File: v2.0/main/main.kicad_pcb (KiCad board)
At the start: 2 copper layers, 61 x 38 mm, 107 parts, among them J1 enc_host, J2 enc_slave, J3 motor_L, J4 motor_R, J5 Battery, J6 enc_host, J7 enc_slave, J8 Conn_ARM_JTAG_SWD_10, J9 Conn_01x02, Q1 LTR-209, Q2 IRLML6402, Q3 BSS138, Q4 LTR-209, Q5 LTR-209, Q6 LTR-209, Q7 PMF250XNEX, Q8 PMF250XNEX, Q9 IRFML8244, SW1 TVAF06-A020B-R, SW2 EG1215AA, SW3 TVAF06-A020B-R, U1 STM32F411CEUx, U2 MA730, U3 ICM-20600, U4 DRV8835, U5 TLV75733PDBV, U6 MA730

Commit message: feat: update pcb routing
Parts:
- removed the C1 at (164.3, 69.3)
- removed the C19 at (163.5, 134.8)
- removed the C2 at (164.3, 71.3)
- removed the D10 at (192.8, 103.8)
- removed the D11 at (193.0, 88.9)
- removed the J1 at (166.8, 103.1)
- removed the J6 at (162.8, 91.2)
- removed L3: 10u, Inductor_SMD:L_0805_2012Metric
- removed the Q7 at (188.0, 88.7)
- removed Q8: PMF250XNEX, Package_TO_SOT_SMD:SOT-323_SC-70_Handsoldering
- removed the R1 at (164.3, 67.3)
- removed the R10 at (159.8, 135.0)
- removed the R23 at (194.4, 100.3)
- removed the R30 at (185.2, 102.6)
- removed the R31 at (186.5, 105.5)
- added C16: 0.1u, Capacitor_SMD:C_0402_1005Metric, F.Cu at (191.1, 94.3)
- added C21: 0.1u, Capacitor_SMD:C_0402_1005Metric, F.Cu at (191.1, 100.5)
- added C22: 0.1u, Capacitor_SMD:C_0402_1005Metric, F.Cu at (177.2, 86.1)
- added C23: 0.1u, Capacitor_SMD:C_0402_1005Metric, F.Cu at (177.1, 110.3)
- added C24: 1u, Capacitor_SMD:C_0402_1005Metric, F.Cu at (177.7, 82.8)
- added C25: 1u, Capacitor_SMD:C_0402_1005Metric, F.Cu at (190.1, 91.3)
- added C8: 0.1u, Capacitor_SMD:C_0201_0603Metric, F.Cu at (152.6, 99.2)
- added D14: OSI5FU3A11C, half_mouse_lib:OSI5FU3A11C, F.Cu at (191.3, 90.5)
- added D15: OSI5FU3A11C, half_mouse_lib:OSI5FU3A11C, F.Cu at (191.4, 103.2)
- added R35: 8.2, Resistor_SMD:R_0402_1005Metric, F.Cu at (189.1, 105.4)
- added R36: 8.2, Resistor_SMD:R_0402_1005Metric, F.Cu at (189.0, 88.0)
- added R4: 1.5k, Resistor_SMD:R_0402_1005Metric, F.Cu at (192.1, 94.3)
- added U7: BCR421UW6-7, Package_TO_SOT_SMD:SOT-23-6, F.Cu at (186.4, 105.8)
- added U8: BCR421UW6-7, Package_TO_SOT_SMD:SOT-23-6, F.Cu at (186.3, 88.4)
- C15: renamed from C16; footprint Capacitor_SMD:C_0603_1608Metric -> Capacitor_SMD:C_0402_1005Metric
- J1, J6: footprint Connector_PinHeader_1.27mm:PinHeader_1x04_P1.27mm_Vertical -> half_mouse_lib:enc_fp
- J2, J7: footprint half_mouse_lib:encoder_board -> half_mouse_lib:enc_board
- J3, J4: footprint half_mouse_lib:motor_SMD -> Connector_PinHeader_1.00mm:PinHeader_1x02_P1.00mm_Vertical
- J9: footprint Connector_PinSocket_1.27mm:PinSocket_1x02_P1.27mm_Vertical -> Connector_PinHeader_1.00mm:PinHeader_1x02_P1.00mm_Vertical
- Q1, Q4, Q5, Q6: value LTR-209 -> OP505A
- R24, R26: value 1k -> 1.5k; footprint Resistor_SMD:R_0201_0603Metric -> Resistor_SMD:R_0402_1005Metric
- R25, R27, R29, R5: value 1k -> 10k; footprint Resistor_SMD:R_0201_0603Metric -> Resistor_SMD:R_0402_1005Metric
- R28: value 10 -> 1.5k; footprint Resistor_SMD:R_0201_0603Metric -> Resistor_SMD:R_0402_1005Metric
- R7: value 10k -> 6.8k
- R8: value 10k -> 15k
- SP1: footprint omni:STM0440-T-R -> half_mouse_lib:SMT-0440-T-HT-R
- moved D8 56.8 mm to (134.6, 100.8)
- moved D7 55.3 mm to (134.6, 99.3)
- moved R18 54.6 mm to (136.5, 100.8), turned to 180 degrees
- moved R17 53.3 mm to (136.5, 99.3), turned to 180 degrees
- moved R20 52.3 mm to (136.5, 103.7), turned to 180 degrees
- moved R21 52.1 mm to (136.5, 105.2), turned to 180 degrees
- moved D10 51.8 mm to (134.6, 103.7)
- moved D11 51.3 mm to (134.6, 105.2)
- moved D9 43.9 mm to (134.6, 102.2)
- moved D6 43.2 mm to (134.6, 95.5), turned to 0 degrees
- moved R19 41.8 mm to (136.5, 102.2), turned to 180 degrees
- moved R11 41.2 mm to (167.1, 79.5), turned to -90 degrees
- moved R16 41.1 mm to (136.5, 95.5)
- moved J1 37.0 mm to (164.7, 105.4), turned to 180 degrees
- moved R10 36.9 mm to (164.5, 83.2)
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- renumbered C3 to C1, C11 to C10, C12 to C11, C13 to C12, C14 to C13, C15 to C14, C20 to C19, C4 to C2, C21 to C20, C5 to C3, C6 to C4, C7 to C5, C8 to C6, C9 to C7, C10 to C9, D14 to D10, D15 to D11, Q9 to Q7, R2 to R1, R11 to R10, R12 to R11, R13 to R12, R14 to R13, R15 to R14, R16 to R15, R17 to R16, R18 to R17, R19 to R18, R20 to R19, R3 to R2, R37 to R20, R38 to R21, R21 to R22, R22 to R23, R4 to R3, R32 to R30, R33 to R31, R34 to R32, R35 to R33, R36 to R34
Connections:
- J2 pad 2: /encoder_R/s_MISO -> ENC_R_B
- J2 pad 3: /encoder_R/s_MOSI -> ENC_R_A
- J2 pad 4: /encoder_R/s_CS -> /encoder_R/s_GND
- J7 pad 2: /encoder_L/s_MISO -> ENC_L_B
- J7 pad 3: /encoder_L/s_MOSI -> ENC_L_A
- J7 pad 4: /encoder_L/s_CS -> /encoder_L/s_GND
- L2 pad 1: Net-(U4-BOUT2) -> Net-(U4-BOUT1)
- L2 pad 2: Net-(J4-Pin_2) -> Net-(J4-Pin_1)
- Q1 pad 1: +3.3VADC -> +3.3V
- Q1 pad 2: IR_RCV_FL -> Net-(Q1-E)
- Q4 pad 1: +3.3VADC -> +3.3V
- Q4 pad 2: IR_RCV_FR -> Net-(Q4-E)
- Q5 pad 1: +3.3VADC -> +3.3V
- Q5 pad 2: IR_RCV_SL -> Net-(Q5-E)
- Q6 pad 1: +3.3VADC -> +3.3V
- Q6 pad 2: IR_RCV_SR -> Net-(Q6-E)
- R24 pad 1: IR_RCV_SL -> Net-(Q4-E)
- R25 pad 1: IR_RCV_SR -> IR_RCV_FR
- R26 pad 1: IR_LED_F -> Net-(Q5-E)
- R26 pad 2: Net-(Q7-G) -> GND
- R27 pad 1: Net-(Q7-G) -> IR_RCV_SL
- R28 pad 1: Net-(D11-K) -> Net-(Q6-E)
- R28 pad 2: Net-(Q7-D) -> GND
- R29 pad 1: IR_LED_S -> IR_RCV_SR
- R29 pad 2: Net-(Q8-G) -> GND
- U1 pad 16: IR_LED_F -> IR_LED_S
- U1 pad 19: IR_LED_S -> IR_LED_F
- U1 pad 2: USER_LED8 -> USER_LED7
- U1 pad 20: USER_LED1 -> unconnected-(U1-PB2-Pad20)
- U1 pad 21: USER_LED2 -> unconnected-(U1-PB10-Pad21)
- U1 pad 3: USER_LED9 -> USER_LED8
- U1 pad 31: USER_LED3 -> USER_LED1
- U1 pad 32: USER_LED4 -> USER_LED2
- U1 pad 33: USER_SW -> USER_LED3
- U1 pad 38: USER_LED5 -> USER_LED4
- U1 pad 39: USER_LED6 -> USER_LED5
- U1 pad 4: USER_LED10 -> USER_LED9
- U1 pad 40: USER_LED7 -> USER_LED6
- U1 pad 5: /OSC_IN -> USER_LED10
- U1 pad 6: /OSC_OUT -> USER_SW
- U1 pad 9: +3.3VADC -> +3.3V
- U4 pad 4: Net-(J4-Pin_1) -> Net-(U4-BOUT1)
- U4 pad 5: Net-(U4-BOUT2) -> Net-(J4-Pin_2)
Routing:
- net +3.3V: track 0.00 -> 217.4 mm, vias 0 -> 5
- net GND: track 0.00 -> 87.5 mm, vias 0 -> 33
- net Net-(D12-K): track 0.00 -> 57.0 mm
- net NRST: track 0.00 -> 52.0 mm, vias 0 -> 2
- net IR_LED_F: track 0.00 -> 42.5 mm
- net +BATT: track 0.00 -> 41.8 mm
- net IR_RCV_FL: track 0.00 -> 40.8 mm, vias 0 -> 2
- net IR_RCV_FR: track 0.00 -> 38.5 mm, vias 0 -> 2
- net IR_RCV_SL: track 0.00 -> 30.9 mm, vias 0 -> 2
- net IR_LED_S: track 0.00 -> 30.9 mm
- net FAN_MOTOR: track 0.00 -> 29.9 mm
- net USER_LED1: track 0.00 -> 29.9 mm, vias 0 -> 2
- net USER_LED2: track 0.00 -> 28.8 mm, vias 0 -> 2
- net USER_LED3: track 0.00 -> 28.4 mm, vias 0 -> 2
- net USER_SPEAKER: track 0.00 -> 27.2 mm, vias 0 -> 2
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- added copper zone on F.Cu, net +3.3V
- added copper zone on F.Cu, net +BATT
- added copper zone on B.Cu, net GND
- added copper zone on F.Cu, net GND
- removed copper zone on B.Cu, net /encoder_L/s_GND
- removed copper zone on F.Cu, net /encoder_L/s_GND
- removed copper zone on B.Cu, net /encoder_R/s_GND
- removed copper zone on F.Cu, net /encoder_R/s_GND
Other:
- board size 61 x 38 mm -> 68 x 38 mm

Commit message: feat: add vias
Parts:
- moved D15 0.71 mm to (191.4, 102.5)
- moved Q4 0.71 mm to (194.1, 100.2)
- moved R24 0.71 mm to (192.1, 99.8)
- moved R25 0.71 mm to (191.6, 98.3)
- moved C21 0.71 mm to (191.0, 99.8)
- moved C16 0.60 mm to (191.1, 94.9)
- moved C25 0.60 mm to (190.1, 92.0)
- moved D14 0.60 mm to (191.3, 91.1)
- moved Q1 0.60 mm to (194.1, 93.5)
- moved R4 0.60 mm to (192.1, 94.9)
- moved R5 0.60 mm to (191.6, 96.4)
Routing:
- net +3.3V: track 217.4 -> 229.0 mm, vias 5 -> 6
- net GND: track 87.5 -> 95.1 mm, vias 33 -> 218
- net Net-(D14-K): track 14.9 -> 13.5 mm
- net Net-(D12-K): track 57.0 -> 58.0 mm
- net SYS_JTMS_SWDIO: track 13.2 -> 13.9 mm
- net +BATT: track 41.8 -> 42.5 mm
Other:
- outline, holes or cut-outs redrawn

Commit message: fix: parts position
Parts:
- moved R11 4.49 mm to (163.6, 76.8), turned to 180 degrees
- moved R29 4.34 mm to (178.2, 107.5), turned to -90 degrees
- moved C23 4.23 mm to (179.7, 107.0), turned to 0 degrees
- moved J2 3.95 mm to (162.0, 120.4), turned to 180 degrees
- moved J7 3.54 mm to (162.0, 74.4), turned to 0 degrees
- moved C9 3.26 mm to (159.4, 114.4)
- moved R3 3.26 mm to (159.4, 116.5)
- moved U2 3.26 mm to (162.1, 115.5)
- moved C22 2.98 mm to (179.7, 87.8), turned to 0 degrees
- moved C19 2.78 mm to (164.6, 80.4)
- moved R10 2.78 mm to (162.0, 81.9)
- moved U6 2.78 mm to (162.1, 79.3)
- moved R28 2.74 mm to (179.7, 108.0), turned to 180 degrees
- moved R27 2.70 mm to (178.1, 87.3), turned to 90 degrees
- moved R2 2.67 mm to (162.1, 112.9), turned to 180 degrees
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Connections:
- J1 pad 2: ENC_R_A -> ENC_R_B
- J1 pad 3: ENC_R_B -> ENC_R_A
- J2 pad 1: /encoder_R/s_VDD -> /encoder_R/s_GND
- J2 pad 2: ENC_R_B -> /encoder_R/ENC_A_
- J2 pad 3: ENC_R_A -> /encoder_R/ENC_B_
- J2 pad 4: /encoder_R/s_GND -> /encoder_R/s_VDD
- J6 pad 2: ENC_L_A -> ENC_L_B
- J6 pad 3: ENC_L_B -> ENC_L_A
- J7 pad 1: /encoder_L/s_VDD -> /encoder_L/s_GND
- J7 pad 2: ENC_L_B -> /encoder_L/ENC_A_
- J7 pad 3: ENC_L_A -> /encoder_L/ENC_B_
- J7 pad 4: /encoder_L/s_GND -> /encoder_L/s_VDD
- U2 pad 2: ENC_R_A -> /encoder_R/ENC_A_
- U2 pad 6: ENC_R_B -> /encoder_R/ENC_B_
- U6 pad 2: ENC_L_A -> /encoder_L/ENC_A_
- U6 pad 6: ENC_L_B -> /encoder_L/ENC_B_
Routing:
- net /encoder_R/s_GND: track 0.00 -> 15.0 mm, vias 0 -> 18
- net /encoder_R/s_VDD: track 0.00 -> 7.25 mm
- net /encoder_L/s_GND: track 3.84 -> 9.15 mm, vias 4 -> 16
- net /encoder_L/s_VDD: track 1.81 -> 7.02 mm
- net /encoder_R/ENC_B_: track 0.00 -> 5.19 mm
- net /encoder_L/ENC_B_: track 0.00 -> 5.17 mm
- net ENC_L_B: track 10.3 -> 6.73 mm
- net +3.3V: track 229.0 -> 225.5 mm, vias 6 -> 7
- net /encoder_R/ENC_A_: track 0.00 -> 3.34 mm
- net ENC_R_A: track 19.7 -> 16.4 mm
- net /encoder_L/ENC_A_: track 0.00 -> 3.25 mm
- net FAN_MOTOR: track 29.9 -> 32.9 mm
- net Net-(Q2-G): track 6.86 -> 4.16 mm
- net Net-(Q3-D): track 3.54 -> 5.98 mm
- net USER_SPEAKER: track 27.2 -> 29.5 mm
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- added copper zone on B.Cu, net /encoder_L/s_GND
- added copper zone on F.Cu, net /encoder_L/s_GND
- added copper zone on B.Cu, net /encoder_R/s_GND
- added copper zone on F.Cu, net /encoder_R/s_GND
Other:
- board size 68 x 38 mm -> 68 x 48 mm

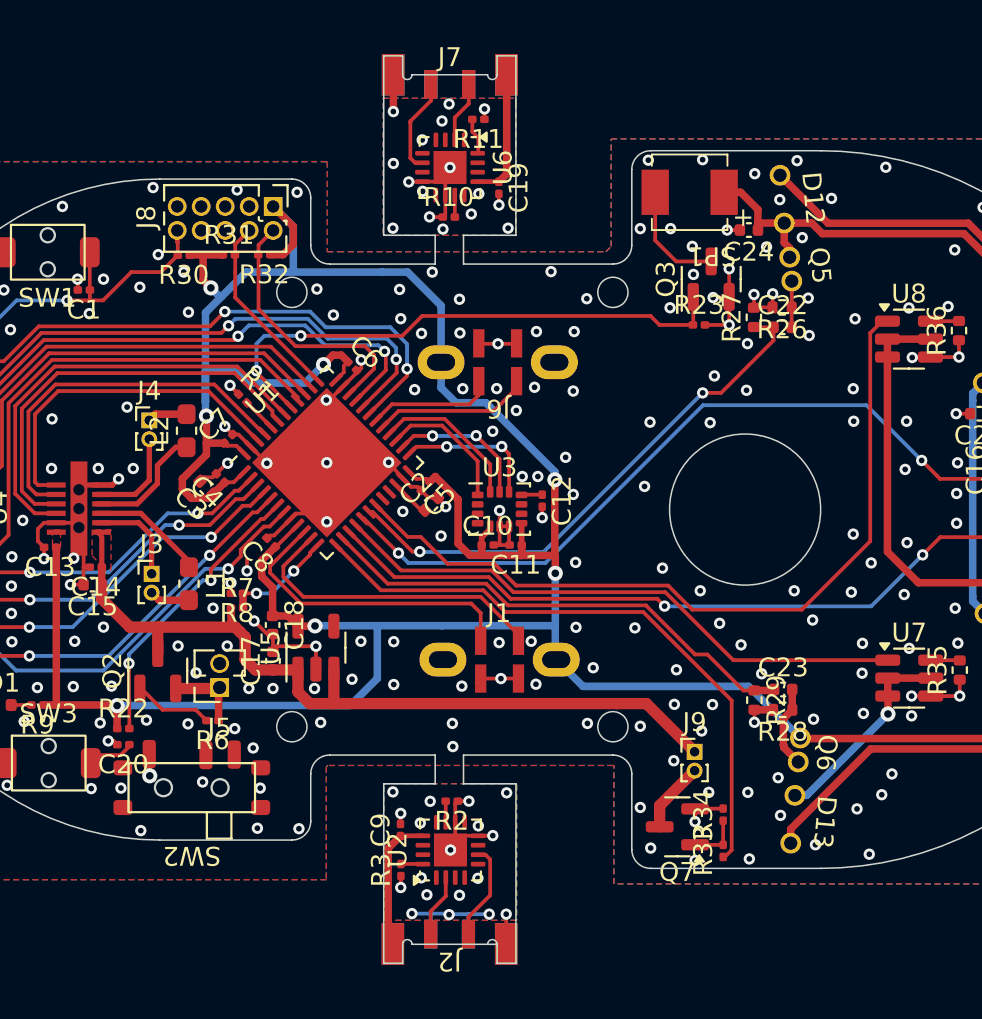
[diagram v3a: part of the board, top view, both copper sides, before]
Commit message: fix: encoder position
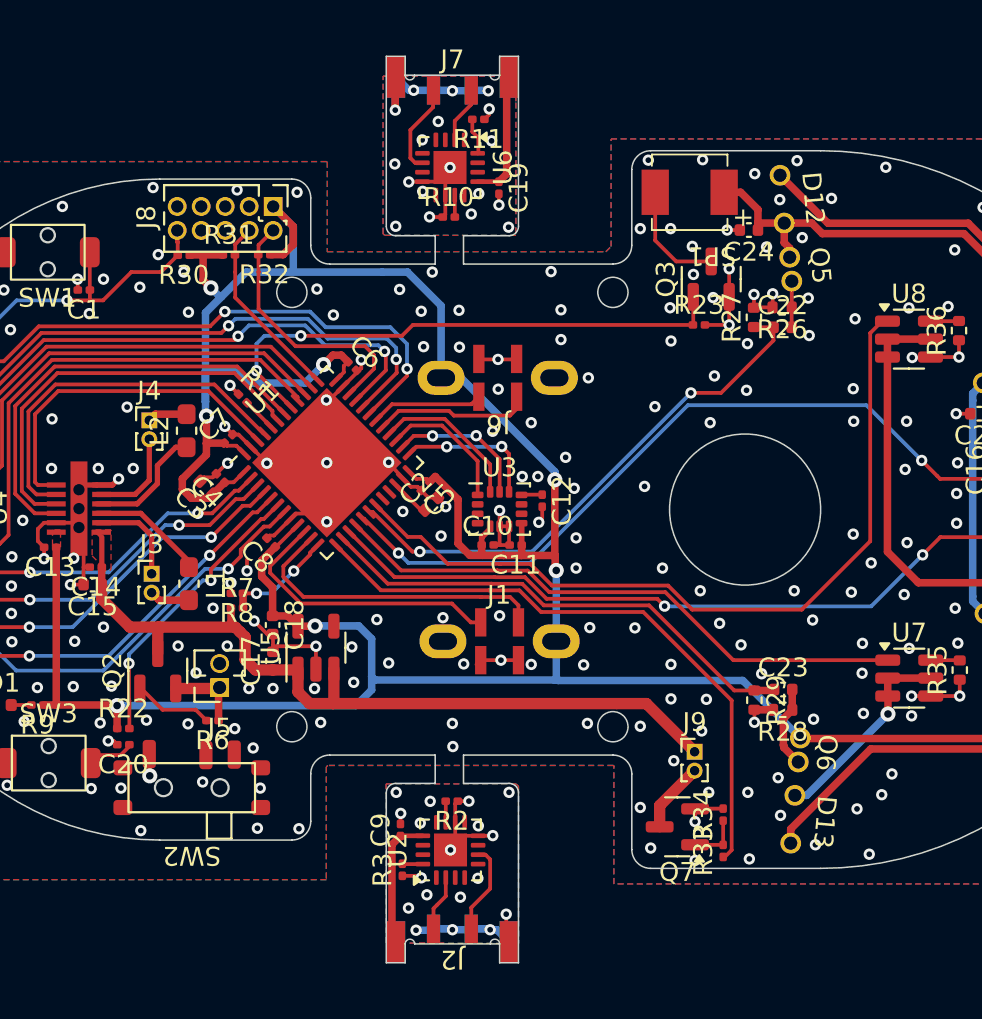
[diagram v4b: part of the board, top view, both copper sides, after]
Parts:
- moved J1 0.98 mm to (164.7, 104.4)
- moved J6 0.83 mm to (164.6, 90.4)
- moved J7 0.18 mm to (162.2, 74.5)
- moved J2 0.18 mm to (162.2, 120.3)
- moved R3 0.08 mm to (159.5, 116.5)
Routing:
- net /encoder_L/s_GND: track 9.15 -> 16.2 mm, vias 16 -> 18
- net ENC_R_A: track 16.4 -> 15.2 mm
- net +3.3V: track 225.5 -> 224.7 mm
- net ENC_L_B: track 6.73 -> 5.96 mm
- net /encoder_R/s_GND: track 15.0 -> 14.4 mm
- net GND: track 96.5 -> 96.9 mm, vias 243 -> 241
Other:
- outline, holes or cut-outs redrawn

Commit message: fix: DRC errors
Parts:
- moved D1 2.76 mm to (135.6, 107.8)
- moved R9 2.75 mm to (137.4, 107.8)
- moved R32 2.45 mm to (149.8, 83.9)
- moved J8 2.45 mm to (150.2, 81.4)
- moved R30 2.45 mm to (145.5, 83.9)
- moved R31 2.45 mm to (147.9, 83.9)
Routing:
- net SYS_JTCK_SWCLK: track 10.2 -> 12.4 mm
- net NRST: track 52.0 -> 50.1 mm
- net Net-(Q2-G): track 4.16 -> 6.00 mm
- net SYS_JTMS_SWDIO: track 14.2 -> 15.8 mm
- net GND: track 96.9 -> 97.9 mm, vias 241 -> 245
- net USER_SW: track 18.0 -> 18.8 mm
- net +3.3V: track 224.7 -> 224.1 mm
- net +BATT: track 44.5 -> 45.1 mm

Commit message: feat: order to JLCPCB
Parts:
- added G***: LOGO, mylib:science_tokyo_logo, B.Cu at (156.3, 97.5)
- C15: footprint Capacitor_SMD:C_0402_1005Metric -> Capacitor_SMD:C_0603_1608Metric
- C19, C9: value 1u -> 0.1u
- R12, R13, R14, R15, R16, R17, R18, R19, R20, R21, R9: value 1k -> 3.3k
- R8: footprint Resistor_SMD:R_0201_0603Metric -> Resistor_SMD:R_0402_1005Metric
- moved C15 0.28 mm to (142.8, 101.4)
- moved R8 0.22 mm to (150.6, 101.8)
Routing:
- net +3.3V: track 224.1 -> 225.0 mm
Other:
- board text added: "2025/02"
- board text added: "R. Terunuma Comet v2"
